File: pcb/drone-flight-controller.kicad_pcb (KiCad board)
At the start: 2 copper layers, 102 x 49 mm, 158 parts, among them J1 SWD, J10 CONN_MANDO, J11 OLED, J12 STM32 SPI, J13 STM32 I2C, J14 STM32 USART, J15 ICSP, J16 USB_B_Micro, J17 Conn_Coaxial, J2 Jumper, J3 USB_B_Micro, J4 CONN_MOT_1, J5 CONN_MOT_2, J6 CONN_MOT_3, J7 CONN_MOT_4, J8 XT-60, J9 LIDAR, SW1 TS24CA_C393942, SW2 TS24CA_C393942, SW3 TS24CA_C393942, SW4 SW_Push_SPDT, U1 STM32F103R8T6, U10 LM7805_TO220, U11 AMS1117-3.3, U2 MPU-6050, U3 ATMEGA328P-AU, U4 CH340G, U5 LM358DR, U6 74HC245, U7 nRF24L01P, U8 MICROSD_C164170, U9 74AHC1G125, Y1 8MHz, Y2 32.768KHz, Y3 16MHz, Y4 12MHz, Y5 16MHz

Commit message: pcb: frame outline placed; sheets resaved by KiCad post-fix
95mm drone frame template placed on the board, and both schematics
re-serialized by KiCad 10's own writer after the save-crash fix -
confirming the canonicalized GND blocks round-trip cleanly.
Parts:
- added REF**: PRUEBA_FRAME_DRONE_95mm, easyeda:FRAME_DRONE_95mm, F.Cu at (152.3, 94.5)
- moved J15 261.0 mm to (92.8, 98.9)
- moved J17 251.6 mm to (102.1, 75.8)
- moved U9 250.4 mm to (100.6, 100.2)
- moved U7 246.3 mm to (111.8, 77.9), turned to 90 degrees
- moved J1 232.5 mm to (128.4, 90.0), turned to -90 degrees
- moved U3 231.2 mm to (112.2, 106.5), turned to 180 degrees
- moved SW3 230.5 mm to (121.1, 114.4), turned to -90 degrees
- moved U6 227.8 mm to (112.2, 89.8), turned to 180 degrees
- moved U8 222.9 mm to (99.0, 89.4), turned to 90 degrees
- moved U1 221.0 mm to (135.3, 101.0)
- moved U4 219.3 mm to (124.8, 80.5)
- moved D3 219.1 mm to (140.4, 77.9), turned to 90 degrees
- moved U5 202.1 mm to (135.0, 83.4), turned to 90 degrees
- moved J16 199.0 mm to (135.0, 72.9), turned to 180 degrees
- moved SW1 191.9 mm to (129.2, 114.4), turned to -90 degrees
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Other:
- copper layers 2 -> 4

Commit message: pcb: sync the TC-6610 THT switch footprints onto the board
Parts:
- SW1, SW2, SW3: value TS24CA_C393942 -> TC-6610_C7528713; footprint easyeda:SW-SMD_2P-TS24CA -> Button_Switch_THT:SW_PUSH_6mm_H9.5mm
- moved SW1 2.77 mm to (130.6, 112.0), turned to 0 degrees
- moved SW3 2.56 mm to (120.3, 111.9), turned to 0 degrees

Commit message: pcb: board work in progress from layout session
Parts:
- moved U3 3.26 mm to (112.0, 103.2)
- moved SW1 1.55 mm to (129.1, 111.9)
- moved SW3 1.35 mm to (118.9, 111.9)
- moved U6 0.94 mm to (112.2, 88.8)
- moved U8 0.38 mm to (99.0, 89.0)
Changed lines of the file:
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@@
 	(footprint "easyeda:TF-SMD_472192001"
 		(layer "F.Cu")
-		(at 98.9936 89.3538 90)
+		(at 99.019 88.9728 90)
 		(property "Reference" "U8"
 			(at 0 -8.15 90)
@@
 	(footprint "Button_Switch_THT:SW_PUSH_6mm_H9.5mm"
 		(layer "F.Cu")
-		(at 120.2702 111.9484)
+		(at 118.924 111.9484)
 		(descr "tactile push button, 6x6mm e.g. PHAP33xx series, height=9.5mm")
 		(tags "tact sw push 6mm")
@@
 	(footprint "Button_Switch_THT:SW_PUSH_6mm_H9.5mm"
 		(layer "F.Cu")
-		(at 130.6068 112.0098)
+		(at 129.0574 111.9378)
 		(descr "tactile push button, 6x6mm e.g. PHAP33xx series, height=9.5mm")
 		(tags "tact sw push 6mm")
@@
 	(footprint "digikey-footprints:TQFP-32_7x7mm"
 		(layer "F.Cu")
-		(at 112.2082 106.4574 180)
+		(at 112.014 103.2002 180)
 		(descr "http://www.atmel.com/Images/Atmel-8826-SEEPROM-PCB-Mounting-Guidelines-Surface-Mount-Packages-ApplicationNote.pdf")
 		(property "Reference" "U3"
@@
 	(footprint "Package_SO:SOIC-20W_7.5x12.8mm_P1.27mm"
 		(layer "F.Cu")
-		(at 112.2408 89.7636 180)
+		(at 112.1936 88.8238 180)
 		(descr "SOIC, 20 Pin (JEDEC MS-013AC, https://www.analog.com/media/en/package-pcb-resources/package/233848rw_20.pdf)")
 		(tags "SOIC SO")

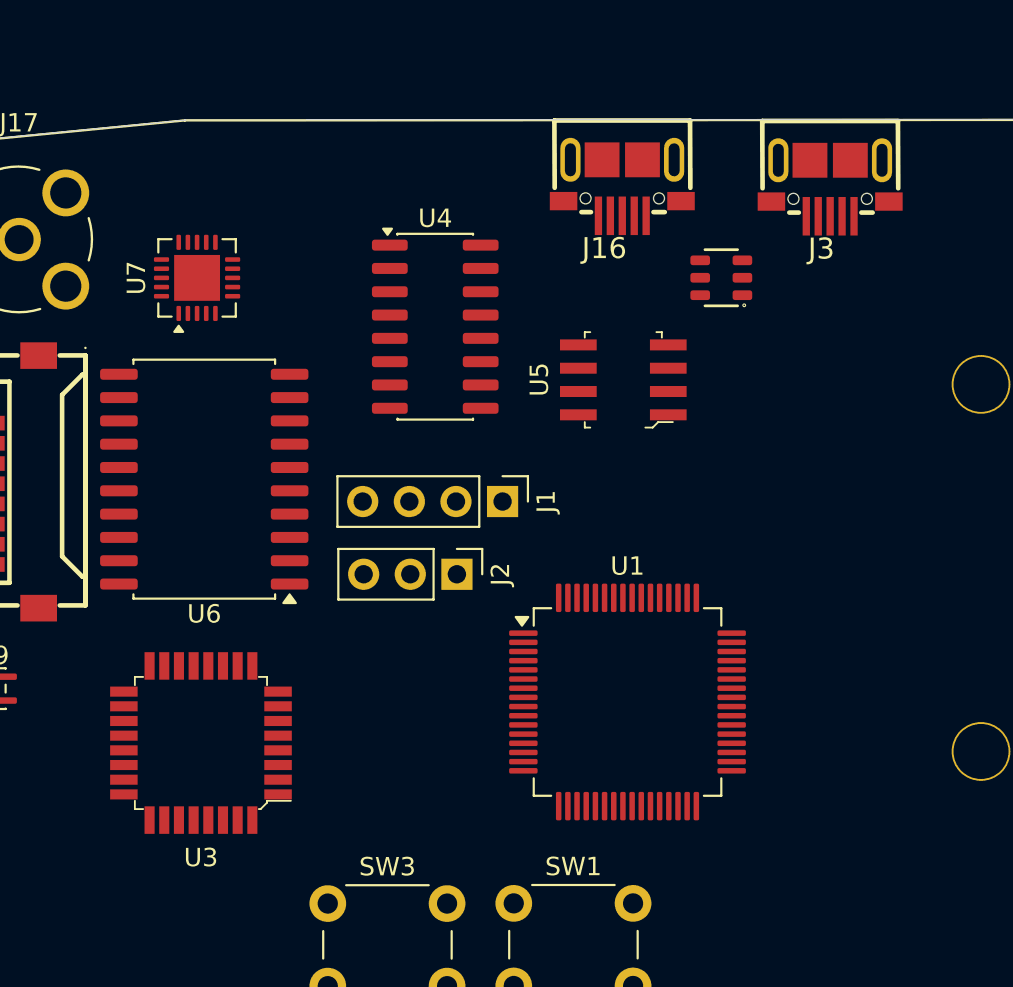
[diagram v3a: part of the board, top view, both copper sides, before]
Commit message: pcb: import the new U3/U5/USB footprints onto the board
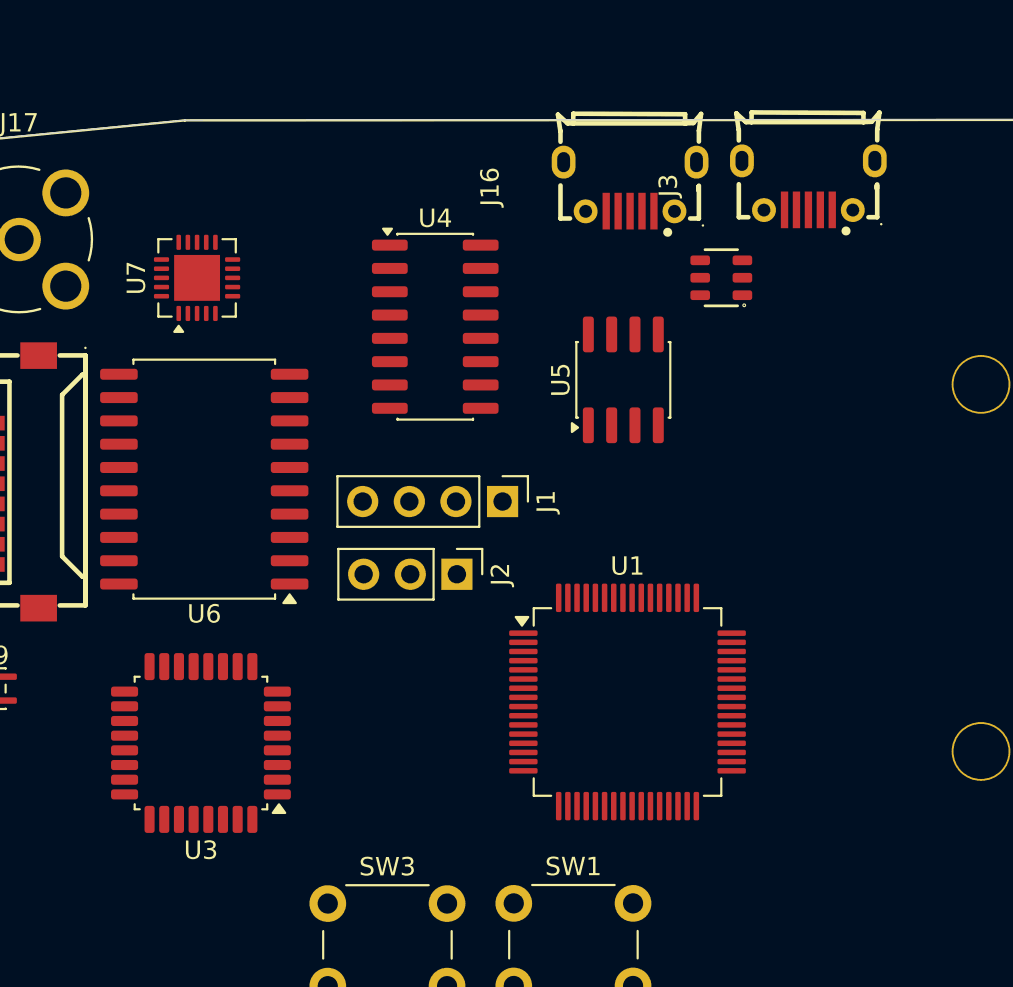
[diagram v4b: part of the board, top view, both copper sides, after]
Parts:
- J16, J3: footprint easyeda:MICRO-USB-SMD_5P-P0.65-H-F_MICRO5.9MMUSB -> easyeda:MICRO-USB-SMD_MICROXNJ_1
- U3: footprint digikey-footprints:TQFP-32_7x7mm -> Package_QFP:TQFP-32_7x7mm_P0.8mm
- U5: footprint digikey-footprints:SOIC-8_W3.9mm -> Package_SO:SOIC-8_3.9x4.9mm_P1.27mm
- moved J3 1.20 mm to (145.1, 72.8), turned to 90 degrees
- moved J16 0.43 mm to (135.4, 72.9), turned to 90 degrees

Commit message: pcb: session state - U10 folded on board, pending sch fixes
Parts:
- U10: footprint Package_TO_SOT_THT:TO-220-3_Vertical -> Package_TO_SOT_THT:TO-220-3_Horizontal_TabDown; moved to B.Cu
- U3: footprint Package_QFP:TQFP-32_7x7mm_P0.8mm -> digikey-footprints:TQFP-32_7x7mm
- U5: footprint Package_SO:SOIC-8_3.9x4.9mm_P1.27mm -> digikey-footprints:SOIC-8_W3.9mm
- moved J13 223.2 mm to (143.2, 96.0)
- moved J12 214.7 mm to (138.0, 112.9), turned to 90 degrees
- moved J14 207.8 mm to (145.6, 116.8), turned to -90 degrees
- moved U2 205.4 mm to (164.8, 89.5), turned to 90 degrees
- moved J9 195.9 mm to (162.1, 116.8), turned to -90 degrees
- moved J10 190.0 mm to (149.8, 103.6), turned to 180 degrees
- moved J7 186.4 mm to (143.8, 92.0), turned to 90 degrees
- moved J6 182.2 mm to (143.8, 88.1), turned to 90 degrees
- moved J5 177.9 mm to (143.9, 84.3), turned to 90 degrees
- moved U10 176.1 mm to (160.8, 106.3), turned to 90 degrees
- moved J4 173.9 mm to (143.9, 80.5), turned to 90 degrees
- moved J11 167.6 mm to (154.5, 93.6), turned to 90 degrees
- moved SW2 155.6 mm to (165.7, 112.1)
- moved U3 6.52 mm to (106.5, 106.7)
- moved SW3 4.27 mm to (114.7, 112.0)
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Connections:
- J14 pad 1: +5V -> GND
- J14 pad 2: USART1_RX -> USART1_TX
- J14 pad 3: USART1_TX -> USART1_RX
- J14 pad 4: GND -> +5V
- J16 pad 6: GND -> (no net)
- J3 pad 6: GND -> (no net)
- J9 pad 1: +5V -> ON_OFF_LIDAR
- J9 pad 2: USART1_TX -> +3.3V
- J9 pad 3: USART1_RX -> GND
- J9 pad 4: GND -> USART1_RX
- J9 pad 5: +3.3V -> USART1_TX
- J9 pad 6: ON_OFF_LIDAR -> +5V

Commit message: pcb: replace U3/U5 board footprints with the official model-bearing ones
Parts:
- U3: footprint digikey-footprints:TQFP-32_7x7mm -> Package_QFP:TQFP-32_7x7mm_P0.8mm
- U5: footprint digikey-footprints:SOIC-8_W3.9mm -> Package_SO:SOIC-8_3.9x4.9mm_P1.27mm
- moved SW4 209.6 mm to (159.8, 79.0)
- moved U11 199.4 mm to (169.0, 98.4)

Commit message: pcb: import the SS12D10G5 footprint onto the board
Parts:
- SW4: value SW_Push_SPDT -> SS12D10G5_C7431054; footprint easyeda:Switch_Slide -> easyeda:SW-TH_SHOU-HAN_SS12D10G4
- moved C35 218.3 mm to (110.1, 77.2), turned to 90 degrees
- moved C37 215.7 mm to (112.9, 73.2)
- moved C36 214.7 mm to (112.9, 74.3)
- moved C34 211.1 mm to (116.7, 78.1), turned to 90 degrees
- moved H7 176.8 mm to (170.0, 114.2)
- moved J8 165.8 mm to (188.8, 92.8), turned to -90 degrees
- moved H5 161.0 mm to (169.9, 72.8), turned to 180 degrees
- moved H2 157.0 mm to (162.4, 114.0)
- moved H8 153.1 mm to (186.0, 72.7), turned to 180 degrees
- moved H6 151.7 mm to (185.2, 114.2)
- moved H1 151.6 mm to (162.2, 72.8), turned to 180 degrees
- moved H4 150.8 mm to (177.5, 114.4)
- moved H3 143.9 mm to (178.4, 72.8), turned to 180 degrees
- moved SW2 47.2 mm to (120.2, 99.6), turned to -90 degrees
- moved SW4 11.0 mm to (152.1, 71.1), turned to 180 degrees
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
